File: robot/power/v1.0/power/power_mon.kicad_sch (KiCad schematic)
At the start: 43 parts, among them J9 Conn_01x02, U11 AD8494

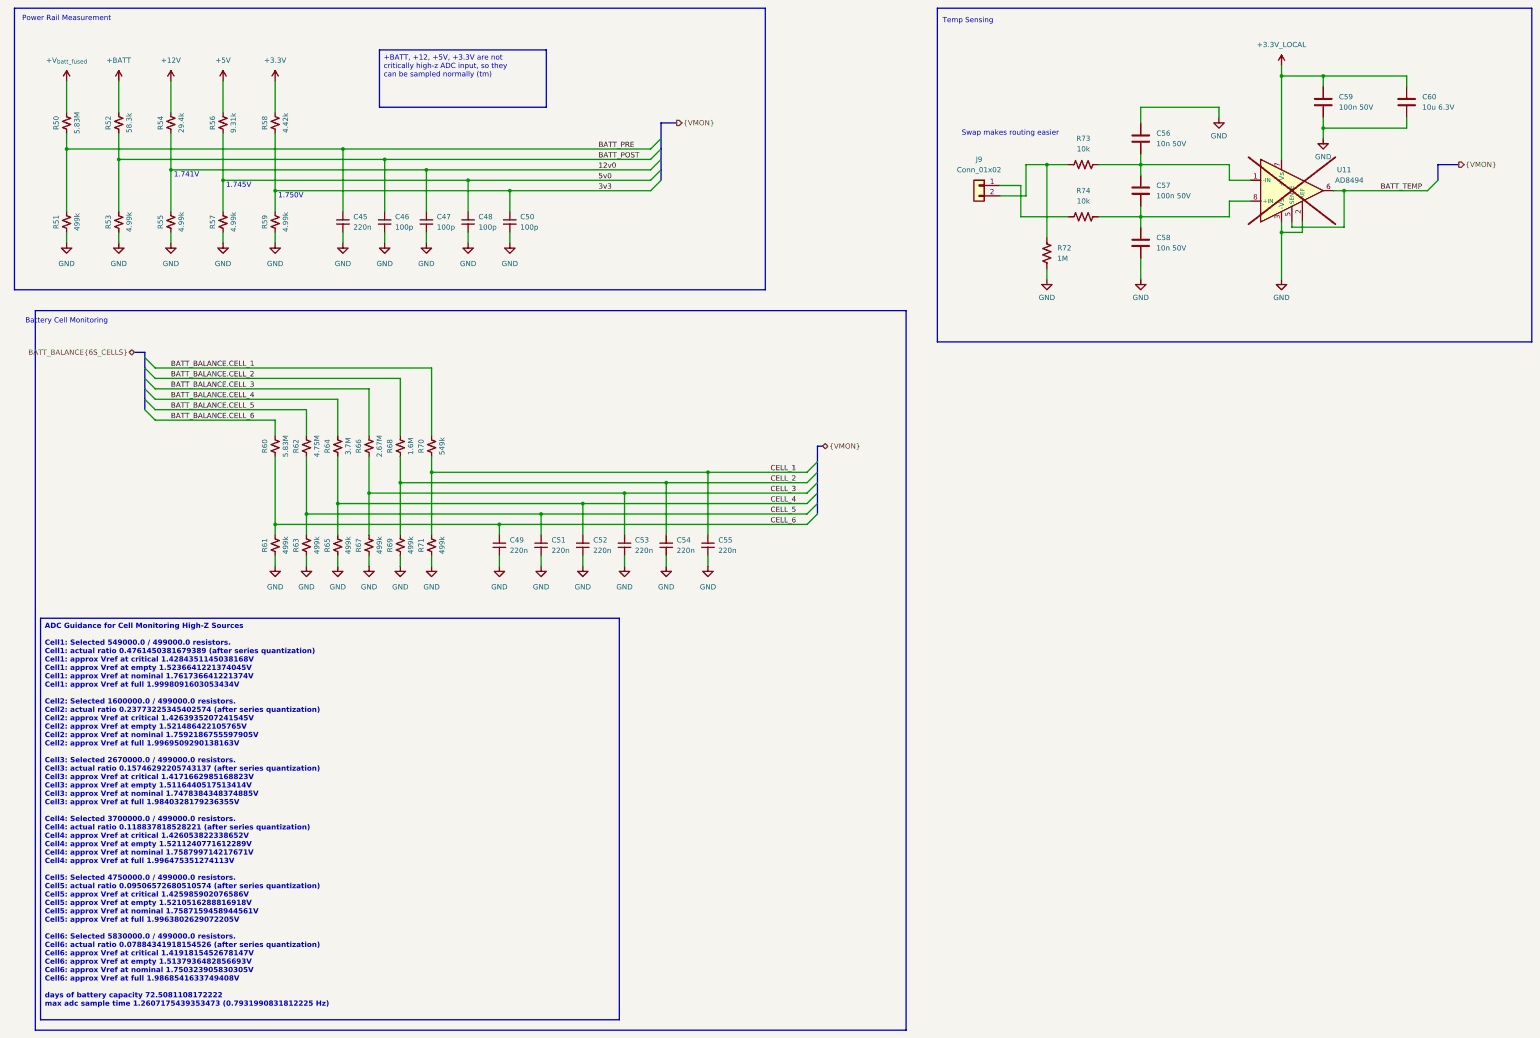
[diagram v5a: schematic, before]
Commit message: power board layout work
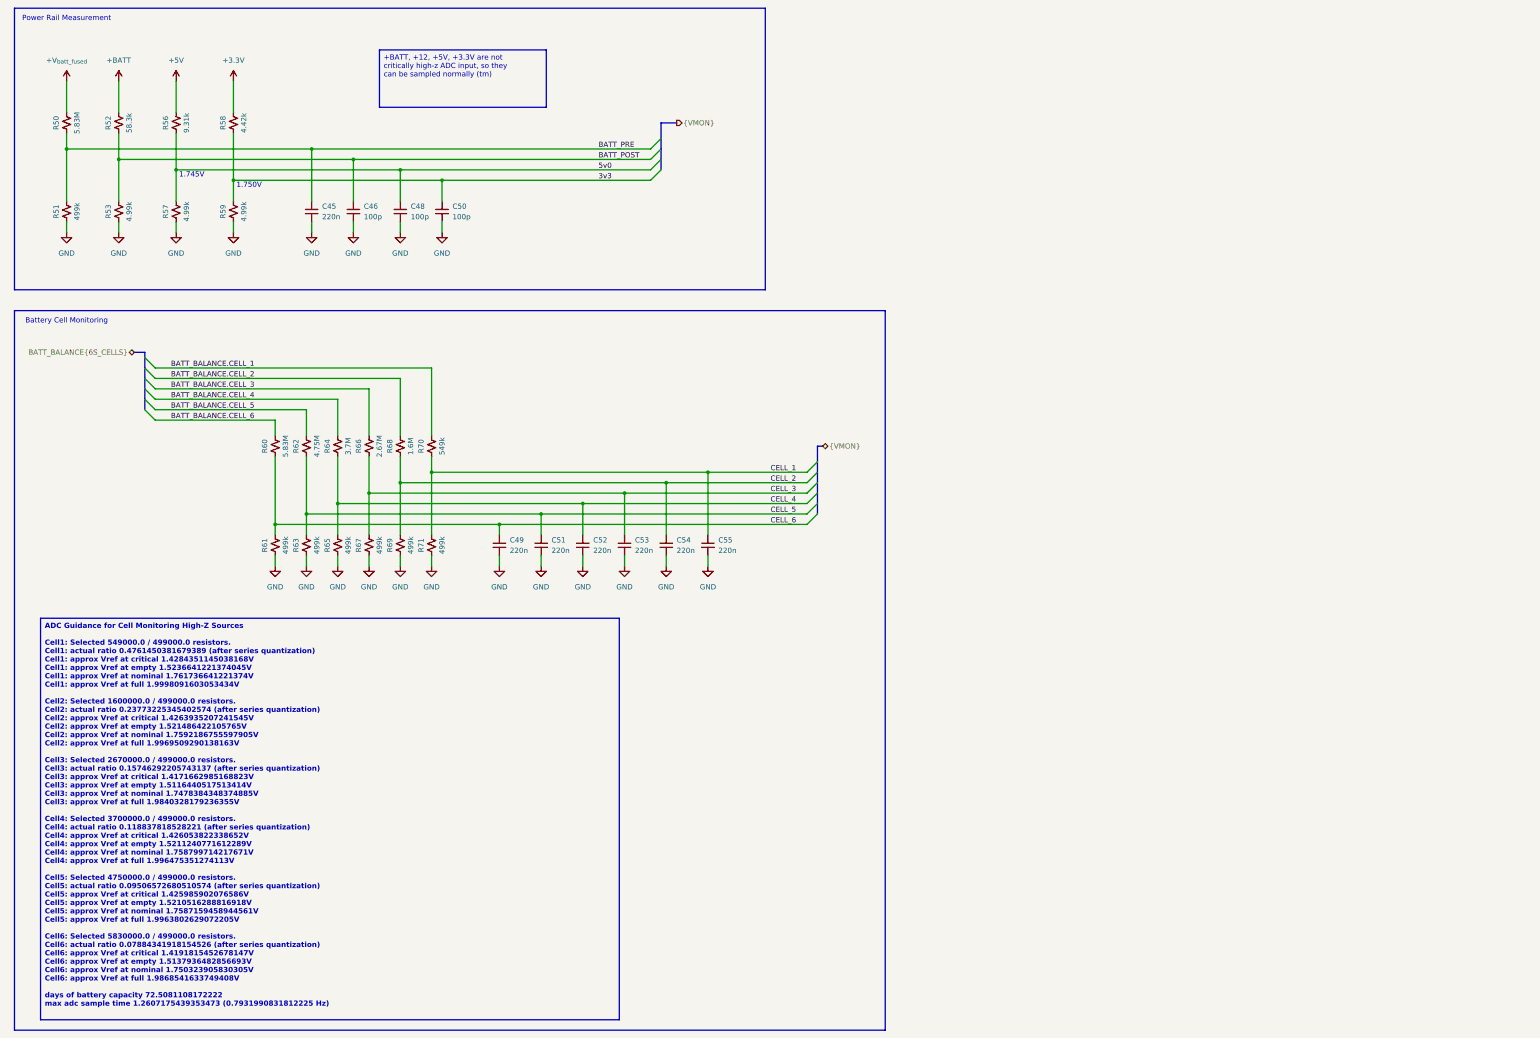
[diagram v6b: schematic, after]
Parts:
- removed C47: 100p, Capacitor_SMD:C_0402_1005Metric, symbol Device:C_Small
- removed C56, C58: 10n 50V, Capacitor_SMD:C_0402_1005Metric, symbol Device:C
- removed C57, C59: 100n 50V, Capacitor_SMD:C_0402_1005Metric, symbol Device:C
- removed C60: 10u 6.3V, Capacitor_SMD:C_1210_3225Metric, symbol Device:C
- removed J9: Conn_01x02, Connector_JST:JST_SH_SM02B-SRSS-TB_1x02-1MP_P1.00mm_Horizontal, symbol Connector_Generic:Conn_01x02
- removed R54: 29.4k, Resistor_SMD:R_0402_1005Metric, symbol Device:R_Small_US
- removed R55: 4.99k, Resistor_SMD:R_0402_1005Metric, symbol Device:R_Small_US
- removed R72: 1M, Resistor_SMD:R_0402_1005Metric, symbol Device:R_US
- removed R73, R74: 10k, Resistor_SMD:R_0402_1005Metric, symbol Device:R_US
- removed U11: AD8494, Package_SO:MSOP-8_3x3mm_P0.65mm, symbol Sensor_Temperature:AD8494
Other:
- note removed: "1.741V"
- note removed: "Swap makes routing easier"
- note removed: "Temp Sensing"
- moved on the sheet: C45, C46, C48, C50, R51, R53, R56, R57, R58, R59

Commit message: production updates
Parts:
- R50, R60: value 5.83M -> 5.6M
- R52: value 58.3k -> 56k
- R64: value 3.7M -> 3.6M
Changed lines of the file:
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@@
 			)
 		)
-		(property "Value" "5.83M"
+		(property "Value" "5.6M"
 			(at 31.75 44.45 90)
 			(effects
@@
 			)
 		)
-		(property "Value" "5.83M"
+		(property "Value" "5.6M"
 			(at 82.55 123.19 90)
 			(effects
@@
 			)
 		)
-		(property "Value" "3.7M"
+		(property "Value" "3.6M"
 			(at 97.79 123.19 90)
 			(effects
@@
 			)
 		)
-		(property "Value" "58.3k"
+		(property "Value" "56k"
 			(at 44.45 44.45 90)
 			(effects
